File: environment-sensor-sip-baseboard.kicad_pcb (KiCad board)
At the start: 4 copper layers, 50 x 26.5 mm, 58 parts, among them J1 USB-C_GCT_USB4105-GF-A, J2 JST_SH_1x4_SM04B-SRSS-TB-LF-SN, J3 JST_SH_1x4_SM04B-SRSS-TB-LF-SN, U1 Antmicro_GEM3, U5 SHT45, U6 BME280

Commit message: [#61553] Route PCB
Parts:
- added TP21: TP_1.5mm_SMD, antmicro-footprints:TP_SMD_1.5mm, F.Cu at (195.9, 138.8)
- added TP22: TP_1.5mm_SMD, antmicro-footprints:TP_SMD_1.5mm, F.Cu at (203.4, 138.8)
- BAT1: moved to B.Cu
- moved TP2 47.9 mm to (190.9, 138.8)
- moved TP13 47.1 mm to (198.4, 138.8)
- moved TP7 47.1 mm to (193.4, 138.8)
- moved LD2 39.2 mm to (174.9, 138.7), turned to 180 degrees
- moved R5 37.3 mm to (174.6, 137.3), turned to 180 degrees
- moved BAT1 33.3 mm to (176.4, 133.0), turned to 180 degrees
- moved TP15 25.5 mm to (168.4, 121.3)
- moved N1 21.8 mm to (173.2, 132.1)
- moved TP9 20.1 mm to (176.0, 116.0)
- moved N2 19.1 mm to (198.1, 131.3)
- moved TP8 17.8 mm to (178.5, 116.0)
- moved TP10 17.1 mm to (173.5, 116.0)
- moved R2 11.2 mm to (176.6, 137.3), turned to 0 degrees
- moved TP14 10.1 mm to (200.9, 138.8)
- moved TP11 4.20 mm to (171.0, 116.0)
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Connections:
- D1 pad 1: GND -> VBUS
- D1 pad 2: VBUS -> GND
- D2 pad 1: GND -> VBUS
- D2 pad 2: VBUS -> GND
- D3 pad 1: GND -> /USB_CC1
- D3 pad 2: /USB_CC1 -> GND
- D4 pad 1: GND -> /USB_CC2
- D4 pad 2: /USB_CC2 -> GND
- D7 pad 1: GND -> +3V3
- D7 pad 2: +3V3 -> GND
- D9 pad 1: GND -> +3V3
- D9 pad 2: +3V3 -> GND
- LD1 pad 1: VBUS -> Net-(LD1-C)
- LD1 pad 2: Net-(LD1-A) -> VBUS
- LD2 pad 1: /LD2 -> Net-(LD2-C)
- LD2 pad 2: Net-(LD2-A) -> /LD2
- R12 pad 2: Net-(LD1-A) -> Net-(LD1-C)
- R5 pad 2: Net-(LD2-A) -> Net-(LD2-C)
- U1 pad A1: unconnected-(U1-PadA1) -> GND
- U1 pad A2: unconnected-(U1-PadA2) -> GND
- U1 pad A3: unconnected-(U1-PadA3) -> GND
- U1 pad A4: unconnected-(U1-PadA4) -> GND
- U1 pad A5: unconnected-(U1-PadA5) -> GND
- U1 pad A6: unconnected-(U1-PadA6) -> GND
- U1 pad B1: unconnected-(U1-PadB1) -> GND
- U1 pad C1: unconnected-(U1-PadC1) -> GND
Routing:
- net /LD2: track 1.40 -> 39.3 mm, vias 1 -> 4
- net +BATT: track 0.70 -> 29.8 mm, vias 1 -> 3
- net /GPIO_PC10: track 0.70 -> 20.3 mm, vias 1 -> 2
- net /USB_MCU_P: track 2.29 -> 21.2 mm
- net /USB_MCU_N: track 2.29 -> 21.2 mm
- net /GPIO_PC12: track 1.40 -> 18.2 mm, vias 1 -> 2
- net /GPIO_PC11: track 0.70 -> 16.7 mm, vias 1 -> 2
- net /CBUS2: track 1.40 -> 15.6 mm, vias 1 -> 2
- net /I2C2_SCL: track 0.70 -> 14.8 mm, vias 1 -> 2
- net /~{FTDI_RESET}: track 1.40 -> 14.8 mm, vias 1 -> 2
- net /CBUS1: track 0.70 -> 13.5 mm, vias 1 -> 2
- net /I2C2_SDA: track 1.40 -> 14.1 mm, vias 1 -> 2
- net GND: track 79.3 -> 91.7 mm, vias 40 -> 42
- net /SPI_CS3: track 0.70 -> 10.4 mm, vias 1 -> 0
- net /I2C_1_SDA: track 64.3 -> 55.0 mm, vias 3 -> 4
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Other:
- board text added: "CBUS1"
- board text added: "CBUS2"
- board text added: "CS2"
- board text added: "CS3"
- board text added: "D+"
- board text added: "D-"
- board text added: "MISO"
- board text added: "MOSI"
- board text added: "PC10"
- board text added: "PC11"
- board text added: "PC12"
- board text added: "Rev.1.0.0 06/2024"
- board text added: "SCK"
- board text added: "SCL"
- board text added: "SDA"
- board text added: "SIP Baseboard"
- board text added: "~{FTDI_RST}"
- board text removed: "A"
- board text removed: "B"
- board text removed: "C"
- board text removed: "Environment Sensor"
- board text removed: "Rev.1.1.0 08/2023"

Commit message: [#61553] Update title block
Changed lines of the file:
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@@
   )
   (paper "A4")
+  (title_block
+    (title "SiP Baseboard")
+    (date "2024-06-28")
+    (rev "1.0.0")
+    (company "Antmicro ")
+    (comment 1 "www.antmicro.com")
+  )
   (layers
     (0 "F.Cu" signal)
@@
     (tags "resistor SMD 0402")
     (property "Author" "Antmicro")
-    (property "DNP" "DNP")
     (property "License" "Apache-2.0")
     (property "MPN" "CR0402-FX-5101GLF")
@@
     (property "ki_description" "SMD Chip Resistor, 5.1 kohm, ± 1%, 63 mW, 0402 [1005 Metric], Thick Film, General Purpose")
     (property "ki_keywords" "0402, SMT, RESISTOR, PASSIVE")
-    (attr smd exclude_from_pos_files exclude_from_bom)
+    (attr smd)
     (fp_text reference "R2" (at -1 -0.55) (layer "F.SilkS")
         (effects (font (size 0.7 0.7) (thickness 0.15)) (justify left bottom))
@@
     (property "ki_description" "SMD Chip Resistor, 100 kohm, ± 1%, 62.5 mW, 0402 [1005 Metric], Thick Film, General Purpose")
     (property "ki_keywords" "0402, SMT, RESISTOR, PASSIVE")
-    (attr smd exclude_from_pos_files exclude_from_bom)
+    (attr smd)
     (fp_text reference "R35" (at -2.465 -3.55 180) (layer "F.SilkS")
         (effects (font (size 0.7 0.7) (thickness 0.15)) (justify left bottom))
@@
     (property "ki_description" "SMD Chip Resistor, 1 Mohm, ± 1%, 62.5 mW, 0402 [1005 Metric], Thick Film, General Purpose")
     (property "ki_keywords" "0402, SMT, RESISTOR, PASSIVE")
-    (attr smd exclude_from_pos_files exclude_from_bom)
+    (attr smd)
     (fp_text reference "R1" (at -2.45 0.4) (layer "F.SilkS")
         (effects (font (size 0.7 0.7) (thickness 0.15)) (justify left bottom))
@@
   (segment (start 207.825 118.125) (end 203.725 118.125) (width 0.15) (layer "In2.Cu") (net 9))
   (segment (start 203.725 118.125) (end 202.8 119.05) (width 0.15) (layer "In2.Cu") (net 9))
+  (segment (start 192.75 119.45) (end 192.75 120.15) (width 0.15) (layer "B.Cu") (net 9))
   (segment (start 193.642 116.558) (end 199.947 116.558) (width 0.15) (layer "B.Cu") (net 9))
-  (segment (start 192.75 119.45) (end 192.75 120.2) (width 0.15) (layer "B.Cu") (net 9))
   (segment (start 202.8 119.05) (end 204.8 119.05) (width 0.15) (layer "B.Cu") (net 9))
   (segment (start 192.8 117.4) (end 193.642 116.558) (width 0.15) (layer "B.Cu") (net 9))
   (segment (start 192.75 119.45) (end 192.8 119.4) (width 0.15) (layer "B.Cu") (net 9))
+  (segment (start 192.75 120.15) (end 200.45 127.85) (width 0.15) (layer "B.Cu") (net 9))
   (segment (start 202.439 119.05) (end 202.8 119.05) (width 0.15) (layer "B.Cu") (net 9))
   (segment (start 192.8 119.4) (end 192.8 117.4) (width 0.15) (layer "B.Cu") (net 9))
-  (segment (start 200.4 127.85) (end 200.45 127.85) (width 0.15) (layer "B.Cu") (net 9))
   (segment (start 199.947 116.558) (end 202.439 119.05) (width 0.15) (layer "B.Cu") (net 9))
-  (segment (start 192.75 120.2) (end 200.4 127.85) (width 0.15) (layer "B.Cu") (net 9))
   (segment (start 185.3 119.5) (end 186 118.8) (width 0.15) (layer "F.Cu") (net 10))
   (segment (start 202.025 117.6) (end 202.55 117.6) (width 0.15) (layer "F.Cu") (net 10))
@@
   (segment (start 209.1 118) (end 208.175 117.075) (width 0.15) (layer "In2.Cu") (net 10))
   (segment (start 203 118.05) (end 204.8 118.05) (width 0.15) (layer "B.Cu") (net 10))
+  (segment (start 192.15 120.85) (end 199.95 128.65) (width 0.15) (layer "B.Cu") (net 10))
   (segment (start 193.449463 116.043) (end 200.214 116.043) (width 0.15) (layer "B.Cu") (net 10))
   (segment (start 200.214 116.043) (end 202.021 117.85) (width 0.15) (layer "B.Cu") (net 10))
   (segment (start 192.15 117.342463) (end 193.449463 116.043) (width 0.15) (layer "B.Cu") (net 10))
   (segment (start 202.021 117.85) (end 202.8 117.85) (width 0.15) (layer "B.Cu") (net 10))
-  (segment (start 192.15 120.5) (end 200.3 128.65) (width 0.15) (layer "B.Cu") (net 10))
+  (segment (start 192.15 118.8) (end 192.15 120.85) (width 0.15) (layer "B.Cu") (net 10))
   (segment (start 202.8 117.85) (end 203 118.05) (width 0.15) (layer "B.Cu") (net 10))
   (segment (start 192.15 118.8) (end 192.15 117.342463) (width 0.15) (layer "B.Cu") (net 10))
-  (segment (start 192.15 118.8) (end 192.15 120.5) (width 0.15) (layer "B.Cu") (net 10))
-  (segment (start 200.3 128.65) (end 201.1 128.65) (width 0.15) (layer "B.Cu") (net 10))
+  (segment (start 199.95 128.65) (end 201.1 128.65) (width 0.15) (layer "B.Cu") (net 10))
   (segment (start 191.15 123.5) (end 192.549999 123.5) (width 0.25) (layer "F.Cu") (net 11))
   (segment (start 194.3 137.4) (end 185.5 137.4) (width 0.15) (layer "F.Cu") (net 11))
@@
   (segment (start 173.7 138.7) (end 181.15 138.7) (width 0.15) (layer "B.Cu") (net 11))
   (segment (start 182.45 137.4) (end 185.5 137.4) (width 0.15) (layer "B.Cu") (net 11))
-  (segment (start 193.6 123.5) (end 192.549999 123.5) (width 0.15) (layer "B.Cu") (net 11))
-  (segment (start 195.3 125.2) (end 193.6 123.5) (width 0.15) (layer "B.Cu") (net 11))
+  (segment (start 195.3 136.4) (end 195.3 125.45) (width 0.15) (layer "B.Cu") (net 11))
   (segment (start 194.45 137.25) (end 195.3 136.4) (width 0.15) (layer "B.Cu") (net 11))
   (segment (start 181.15 138.7) (end 182.45 137.4) (width 0.15) (layer "B.Cu") (net 11))
-  (segment (start 195.3 136.4) (end 195.3 125.2) (width 0.15) (layer "B.Cu") (net 11))
+  (segment (start 195.3 125.45) (end 193.35 123.5) (width 0.15) (layer "B.Cu") (net 11))
+  (segment (start 193.35 123.5) (end 192.549999 123.5) (width 0.15) (layer "B.Cu") (net 11))
   (segment (start 180.75 127.4) (end 179.35 127.4) (width 0.25) (layer "F.Cu") (net 15))
   (via (at 179.35 127.4) (size 0.6) (drill 0.25) (layers "F.Cu" "B.Cu") (net 15))

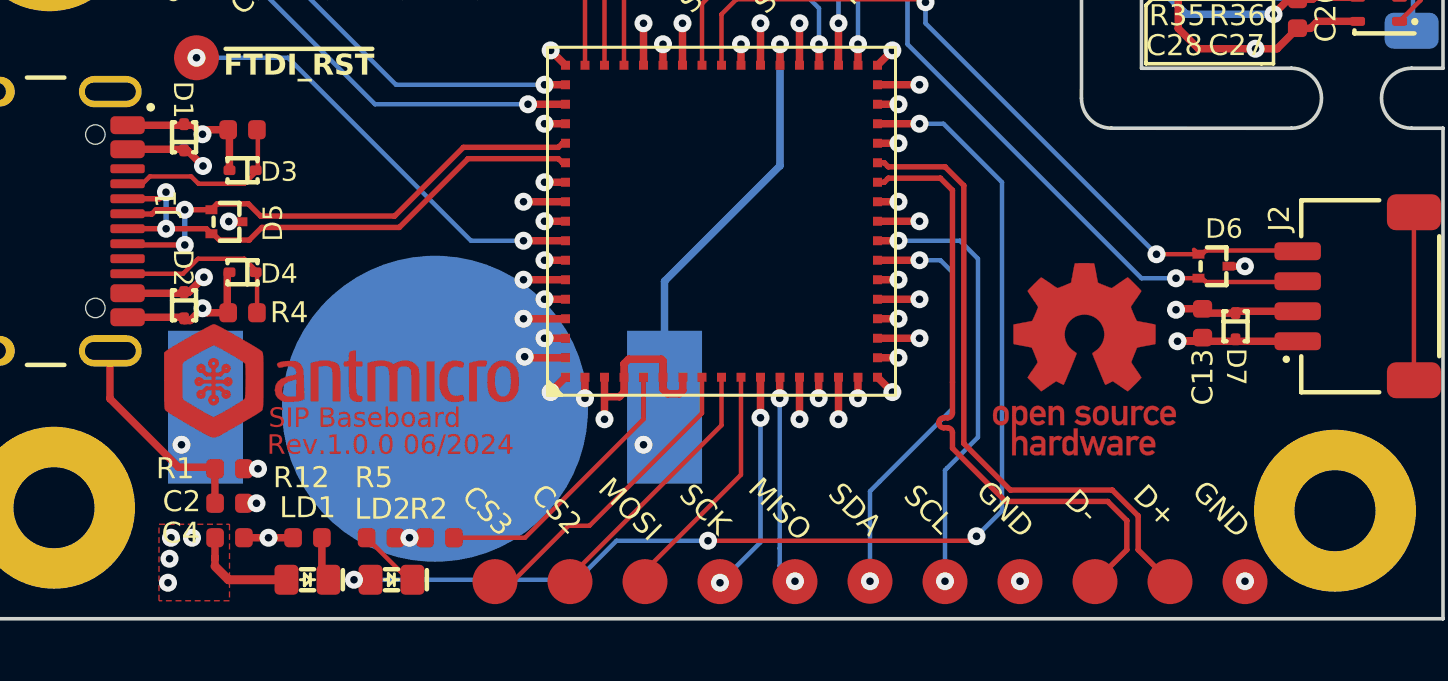
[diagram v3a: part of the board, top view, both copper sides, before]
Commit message: [#61553] Fix logo at PCB
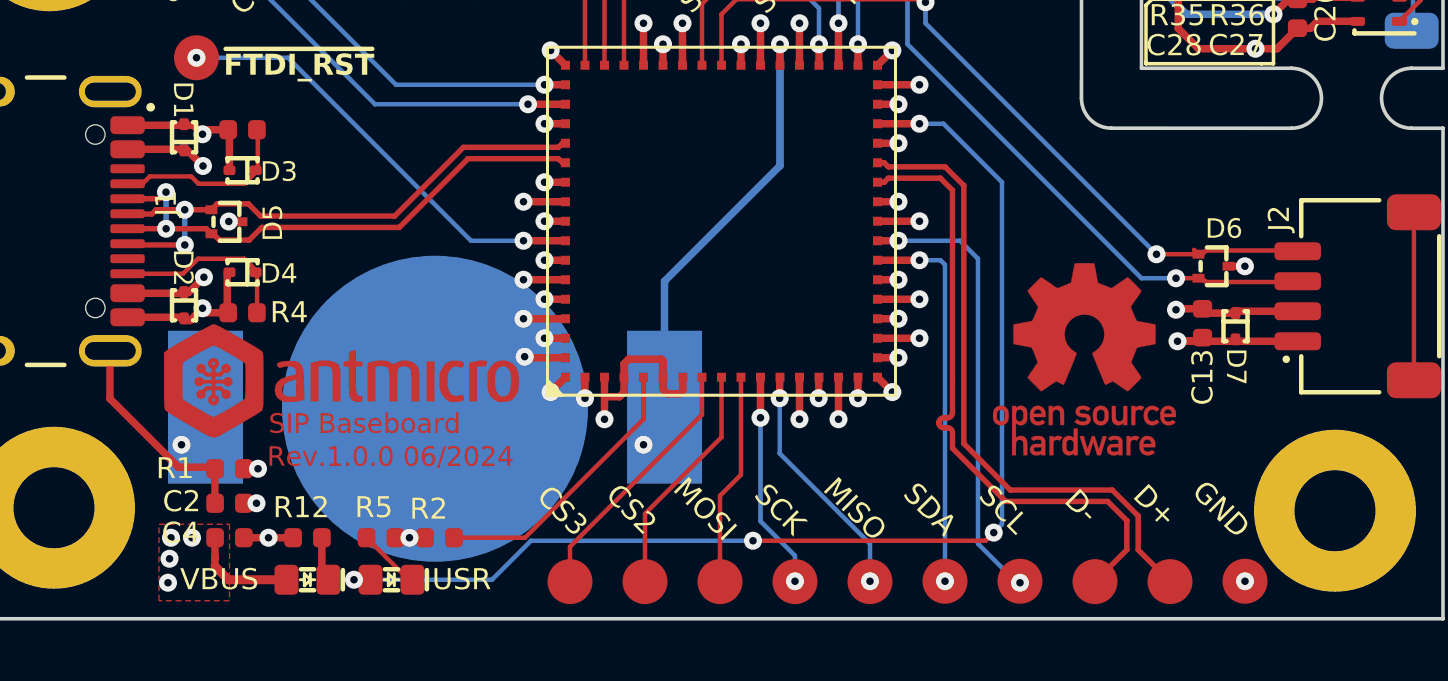
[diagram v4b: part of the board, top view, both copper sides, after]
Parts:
- removed TP22: TP_1.5mm_SMD, antmicro-footprints:TP_SMD_1.5mm
- moved TP21 7.50 mm to (203.4, 138.8)
- moved TP7 2.50 mm to (195.9, 138.8)
- moved TP16 2.50 mm to (180.9, 138.8)
- moved TP17 2.50 mm to (183.4, 138.8)
- moved TP18 2.50 mm to (185.9, 138.8)
- moved TP19 2.50 mm to (188.4, 138.8)
- moved TP2 2.50 mm to (193.4, 138.8)
- moved TP20 2.50 mm to (190.9, 138.8)
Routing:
- net /SPI_CS3: track 10.4 -> 8.87 mm
- net /SPI_CS2: track 9.21 -> 7.91 mm
- net /I2C2_SDA: track 14.1 -> 12.9 mm
- net /SPI2_MOSI: track 8.33 -> 7.10 mm
- net /SPI2_MISO: track 7.01 -> 8.05 mm
- net GND: vias 42 -> 41
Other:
- board text added: "USR"
- board text added: "VBUS"
